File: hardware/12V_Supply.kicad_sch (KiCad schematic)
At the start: 26 parts, among them J4003 6490XX227222_649006227222, J4005 6490XX227222_649006227222, J4006 6490XX227222_649006227222

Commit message: feat(schematic): added cooler mounting holes
added cooler mounting holes to schematic
changed temp pins to read proper tempurature
small fixes
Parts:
- removed C1, C4014, C4015: 330uF, Capacitor_SMD:C_0805_2012Metric, symbol Device:C
- removed C4001, C4002, C4003: 470uF, Capacitor_SMD:C_0805_2012Metric, symbol Device:C
- C4004, C4005, C4006: footprint Capacitor_SMD:C_0805_2012Metric -> Capacitor_SMD:C_1210_3225Metric
- C4007, C4008, C4009: footprint Capacitor_SMD:C_0805_2012Metric -> Capacitor_SMD:C_0603_1608Metric
- C4010, C4011, C4012: footprint Capacitor_SMD:C_0805_2012Metric -> Capacitor_SMD:C_0402_1005Metric
- C4016, C4017, C4018: footprint Capacitor_THT:CP_Radial_D8.0mm_P3.50mm -> Capacitor_SMD:CP_Elec_8x10.5
- D4001: footprint LED_SMD:LED_0805_2012Metric_Pad1.15x1.40mm_HandSolder -> LED_SMD:LED_0603_1608Metric

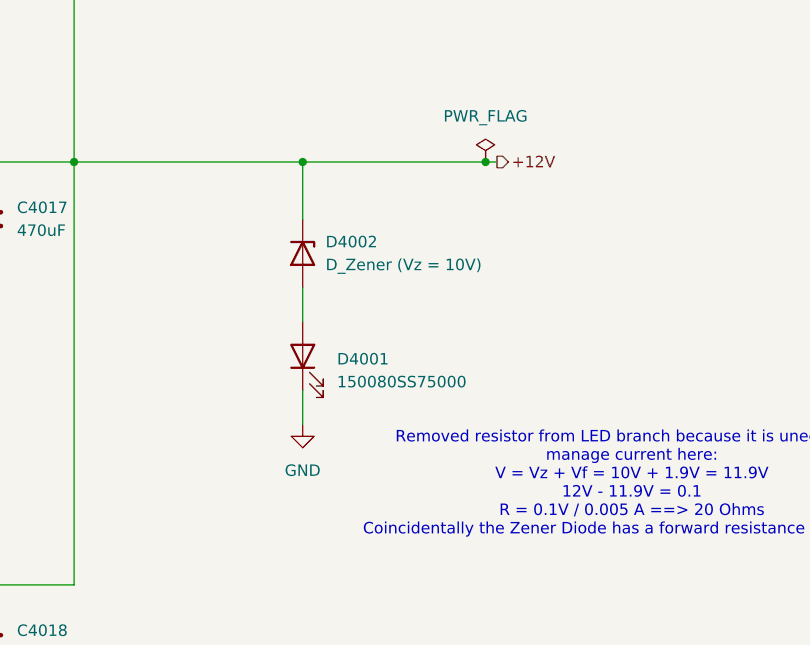
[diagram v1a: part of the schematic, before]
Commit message: feat(hardware): microcontroller routing
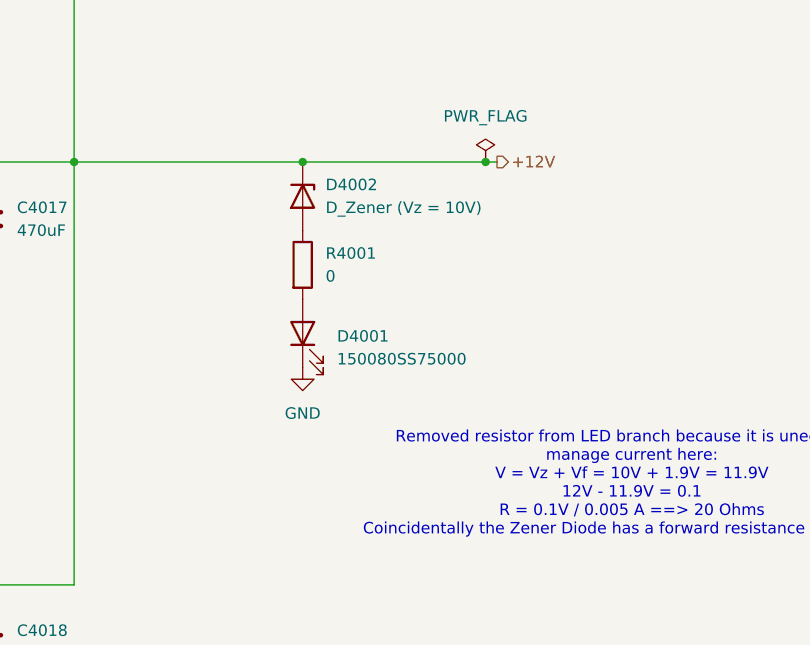
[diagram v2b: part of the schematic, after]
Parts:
- added R4001: 0, Resistor_SMD:R_0805_2012Metric, symbol Device:R
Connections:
- net at D4001.2 (A): now also R4001.2; no longer D4002.2 (A)
- new net: D4002.2 (A), R4001.1
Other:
- moved on the sheet: D4001, D4002

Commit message: chore(schematic): add LCSC Part Numbers
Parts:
- C4004, C4005, C4006: LCSC Part Number (none) -> C77101
- C4007, C4008, C4009: LCSC Part Number (none) -> C70225
- C4010, C4011, C4012: LCSC Part Number (none) -> C1581
- C4016, C4017, C4018: LCSC Part Number (none) -> C65223
- D4001: LCSC Part Number (none) -> C2286
- J4003, J4005, J4006: LCSC Part Number (none) -> C586651
- L4001, L4002, L4003: LCSC Part Number (none) -> C1331996
- R4001: LCSC Part Number (none) -> C17477
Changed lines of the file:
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@@
+			)
+		)
+		(property "LCSC Part Number" "C1581"
+			(at 127 147.32 0)
+			(effects
+				(font
+					(size 1.27 1.27)
+				)
+				(hide yes)
 			)
 		)
@@
 			)
 		)
+		(property "LCSC Part Number" "C586651"
+			(at 40.64 44.45 0)
+			(effects
+				(font
+					(size 1.27 1.27)
+				)
+				(hide yes)
+			)
+		)
 		(pin "6"
 		)
@@
 			)
 		)
+		(property "LCSC Part Number" "C77101"
+			(at 100.33 100.33 0)
+			(effects
+				(font
+					(size 1.27 1.27)
+				)
+				(hide yes)
+			)
+		)
 		(pin "1"
 		)
@@
 			)
 		)
+		(property "LCSC Part Number" "C586651"
+			(at 43.18 138.43 0)
+			(effects
+				(font
+					(size 1.27 1.27)
+				)
+				(hide yes)
+			)
+		)
 		(pin "6"
 		)
@@
 			)
 		)
+		(property "LCSC Part Number" "C65223"
+			(at 167.64 100.33 0)
+			(effects
+				(font
+					(size 1.27 1.27)
+				)
+				(hide yes)
+			)
+		)
 		(pin "1"
 		)
@@
 			)
 		)
+		(property "LCSC Part Number" "C70225"
+			(at 111.76 147.32 0)
+			(effects
+				(font
+					(size 1.27 1.27)
+				)
+				(hide yes)
+			)
+		)
 		(pin "1"
 		)
@@
 			)
 		)
+		(property "LCSC Part Number" "C2286"
+			(at 203.2 113.03 0)
+			(effects
+				(font
+					(size 1.27 1.27)
+				)
+				(hide yes)
+			)
+		)
 		(pin "2"
 		)
@@
 		)
 		(property "Description" ""
+			(at 40.64 92.71 0)
+			(effects
+				(font
+					(size 1.27 1.27)
+				)
+				(hide yes)
+			)
+		)
+		(property "LCSC Part Number" "C586651"
 			(at 40.64 92.71 0)
 			(effects
@@
 			)
 		)
+		(property "LCSC Part Number" "C1581"
+			(at 127 53.34 0)
+			(effects
+				(font
+					(size 1.27 1.27)
+				)
+				(hide yes)
+			)
+		)
 		(pin "1"
 		)
@@
 		)
 		(property "Description" "Unpolarized capacitor"
+			(at 127 100.33 0)
+			(effects
+				(font
+					(size 1.27 1.27)
+				)
+				(hide yes)
+			)
+		)
+		(property "LCSC Part Number" "C1581"
 			(at 127 100.33 0)
 			(effects
@@
 			)
 		)
+		(property "LCSC Part Number" "C65223"
+			(at 167.64 53.34 0)
+			(effects
+				(font
+					(size 1.27 1.27)
+				)
+				(hide yes)
+			)
+		)
 		(pin "1"
 		)
@@
 			)
 		)
+		(property "LCSC Part Number" "C1331996"
+			(at 138.43 140.97 0)
+			(effects
+				(font
+					(size 1.27 1.27)
+				)
+				(hide yes)
+			)
+		)
 		(pin "2"
 		)
@@
 			)
 		)
+		(property "LCSC Part Number" "C65223"
+			(at 167.64 147.32 0)
+			(effects
+				(font
+					(size 1.27 1.27)
+				)
+				(hide yes)
+			)
+		)
 		(pin "1"
 		)
@@
 			)
 		)
+		(property "LCSC Part Number" ""
+			(at 203.2 97.79 0)
+			(effects
+				(font
+					(size 1.27 1.27)
+				)
+				(hide yes)
+			)
+		)
 		(pin "1"
 		)
@@
 			)
 		)
+		(property "LCSC Part Number" "C1331996"
+			(at 138.43 46.99 0)
+			(effects
+				(font
+					(size 1.27 1.27)
+				)
+				(hide yes)
+			)
+		)
 		(pin "2"
 		)
@@
 			)
 		)
+		(property "LCSC Part Number" "C70225"
+			(at 111.76 53.34 0)
+			(effects
+				(font
+					(size 1.27 1.27)
+				)
+				(hide yes)
+			)
+		)
 		(pin "1"
 		)
@@
 			)
 		)
+		(property "LCSC Part Number" "C70225"
+			(at 111.76 100.33 0)
+			(effects
+				(font
+					(size 1.27 1.27)
+				)
+				(hide yes)
+			)
+		)
 		(pin "1"
 		)
@@
 			)
 		)
+		(property "LCSC Part Number" "C77101"
+			(at 100.33 147.32 0)
+			(effects
+				(font
+					(size 1.27 1.27)
+				)
+				(hide yes)
+			)
+		)
 		(pin "1"
 		)
@@
 			)
 		)
+		(property "LCSC Part Number" "C77101"
+			(at 100.33 53.34 0)
+			(effects
+				(font
+					(size 1.27 1.27)
+				)
+				(hide yes)
+			)
+		)
 		(pin "1"
 		)
@@
 		)
 		(property "Description" "Inductor"
+			(at 138.43 93.98 0)
+			(effects
+				(font
+					(size 1.27 1.27)
+				)
+				(hide yes)
+			)
+		)
+		(property "LCSC Part Number" "C1331996"
 			(at 138.43 93.98 0)
 			(effects
@@
 			(at 203.2 105.41 0)
 			(effects
+				(font
+					(size 1.27 1.27)
+				)
+				(hide yes)
+			)
+		)
+		(property "LCSC Part Number" "C17477"
+			(at 203.2 105.41 0)
+			(effects
